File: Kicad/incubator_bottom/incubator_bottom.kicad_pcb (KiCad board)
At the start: 2 copper layers, 99.9 x 73.7 mm, 52 parts, among them J1 Conn_01x02, J10 Conn_01x01, J11 Conn_01x01, J12 Conn_01x01, J2 Conn_02x03_Odd_Even, J4 Conn_01x01, J5 AudioJack3_SwitchTR, J6 AudioJack3_SwitchTR, J7 Conn_01x01, J8 Conn_01x06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

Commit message: fix: PWM for PID
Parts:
- removed logoHackuarium: , Incubator:logoHackuarium
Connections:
- U3 pad 10: FAN -> PID
- U3 pad 11: PID -> D7
- U3 pad 9: D5 -> FAN
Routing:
- net PID: track 121.6 -> 117.6 mm
- net FAN: track 36.1 -> 34.9 mm

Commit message: feat: v1.0.1 of board
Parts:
- added D6: GREEN, LED_SMD:LED_0805_2012Metric_Pad1.15x1.40mm_HandSolder, F.Cu at (95.2, -45.2)
- added D7: RED, LED_SMD:LED_0805_2012Metric_Pad1.15x1.40mm_HandSolder, F.Cu at (97.7, -46.9)
- added R14: 10k, Resistor_SMD:R_0805_2012Metric_Pad1.20x1.40mm_HandSolder, F.Cu at (95.2, -41.0)
- added R15: 10k, Resistor_SMD:R_0805_2012Metric_Pad1.20x1.40mm_HandSolder, F.Cu at (97.7, -41.0)
- added logoHackuarium: , Incubator:logoHackuarium, B.Cu at (86.9, -54.1)
- added logoHackuarium: , Incubator:logoHackuarium, F.Cu at (0.25, -18.9)
- moved C5 7.87 mm to (83.1, -23.6), turned to 270 degrees
- moved H6 2.72 mm to (31.2, -25.6)
- moved H8 2.72 mm to (71.3, -25.6)
- moved JP1 2.43 mm to (81.7, -31.5)
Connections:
- net SCK renamed SCK|MONITORING
- C5 pad 2: GND -> Net-(C5-Pad2)
- J8 pad 1: ~RESET -> Net-(C5-Pad2)
- U3 pad 14: Net-(U3-Pad14) -> ERROR
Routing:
- net ERROR: track 0.00 -> 9.71 mm
- net ~RESET: track 36.1 -> 29.1 mm
- net 12V: track 190.2 -> 184.8 mm
- net Net-(C5-Pad2): track 0.00 -> 5.33 mm
- net Net-(D7-Pad2): track 0.00 -> 3.80 mm
- net ONE-WIRE-2: track 118.2 -> 114.5 mm, vias 4 -> 3
- net SCK|MONITORING: track 20.1 -> 23.5 mm
- net VIN: track 254.1 -> 251.0 mm
- net Net-(D6-Pad2): track 0.00 -> 2.16 mm
- net MOSI: track 19.5 -> 21.0 mm
- net TX: track 14.0 -> 15.3 mm
- net GND: track 9.93 -> 9.51 mm, vias 45 -> 49
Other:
- board text added: "ERR"
- board text added: "Incubator V 1.0.1"
- board text added: "MON"
- board text removed: "Incubator V 1.0.0"

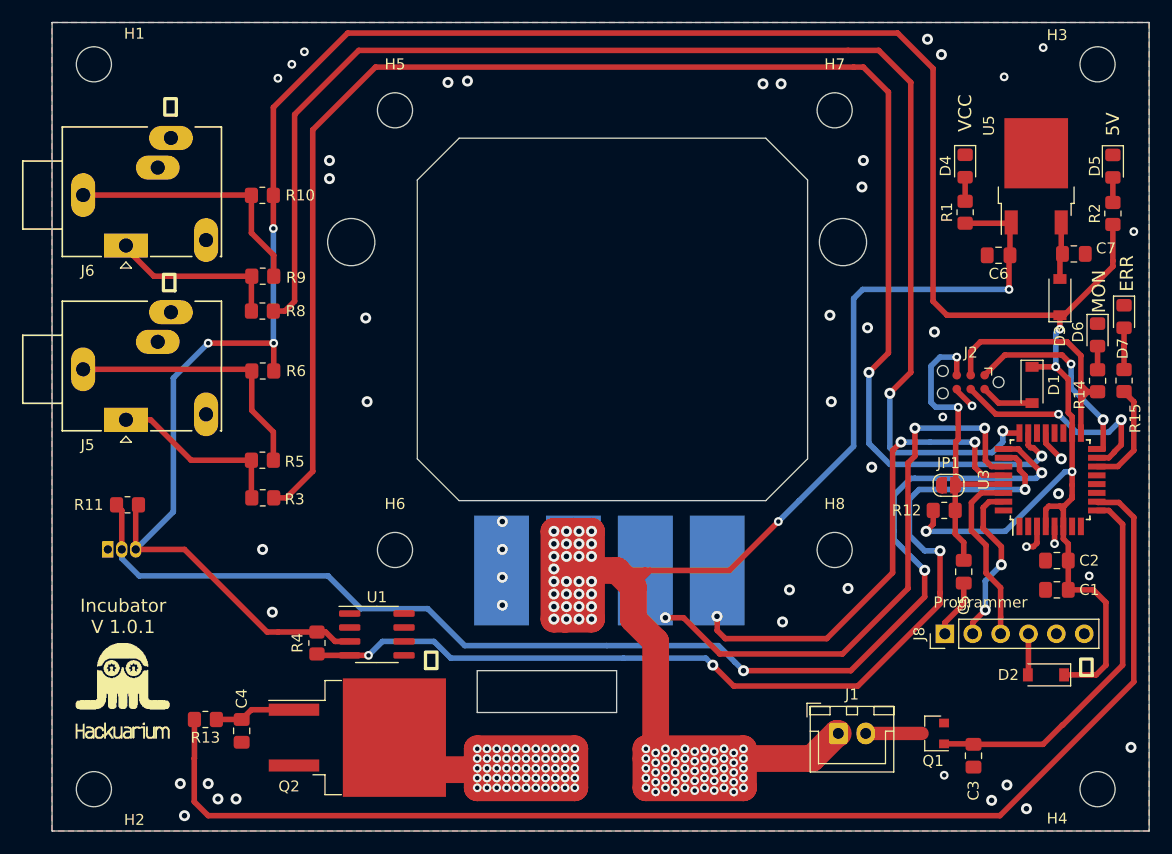
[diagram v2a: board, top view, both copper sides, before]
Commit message: fix: solve issue for holes diameter
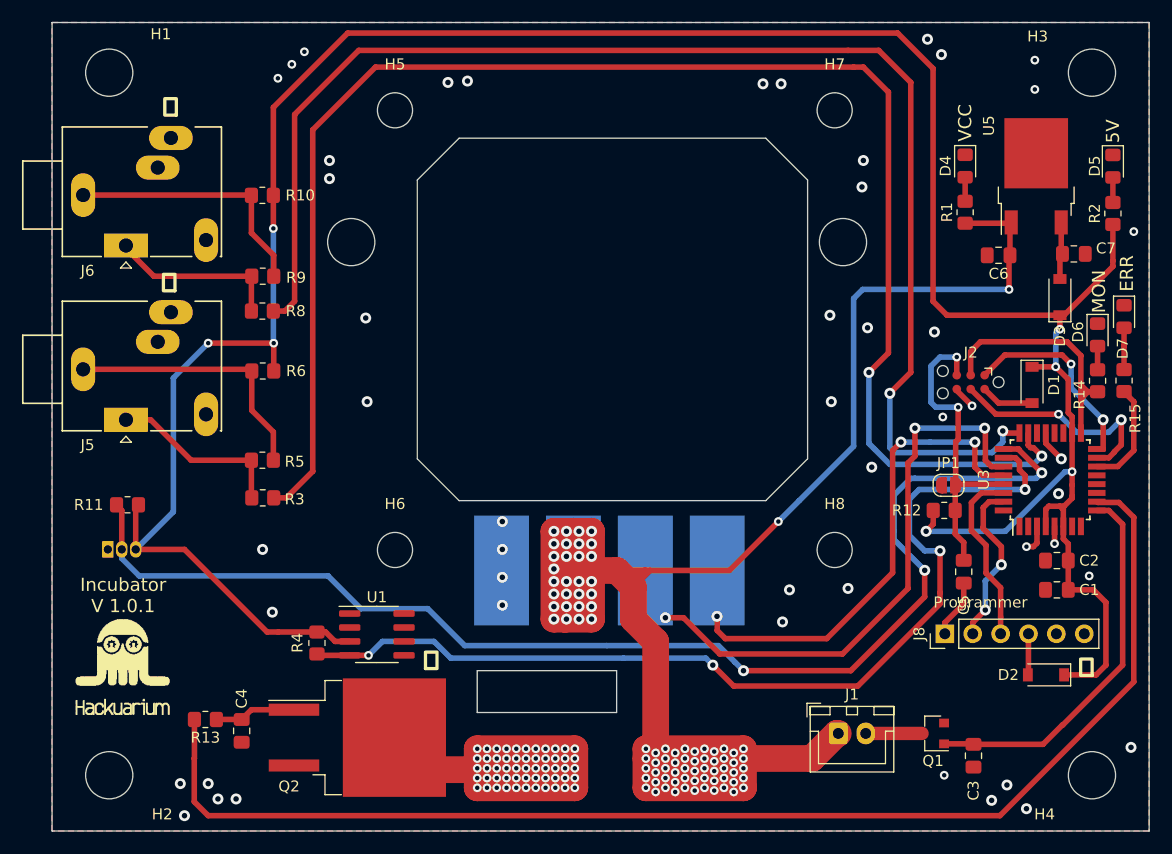
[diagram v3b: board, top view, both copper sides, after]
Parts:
- H1, H2, H3, H4: footprint MountingHole:MountingHole_3.2mm_M3 -> MountingHole:MountingHole_4.3mm_M4
- moved logoHackuarium 2.16 mm to (0.25, -21.1)
- moved H2 1.89 mm to (5.21, -5.08)
- moved H1 1.59 mm to (5.21, -69.1)
- moved H4 1.37 mm to (94.7, -5.08)
- moved H3 0.92 mm to (94.7, -69.1)

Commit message: fix: version 1.0.2 of the PCB change size holes M4 -> M3 and changes their position
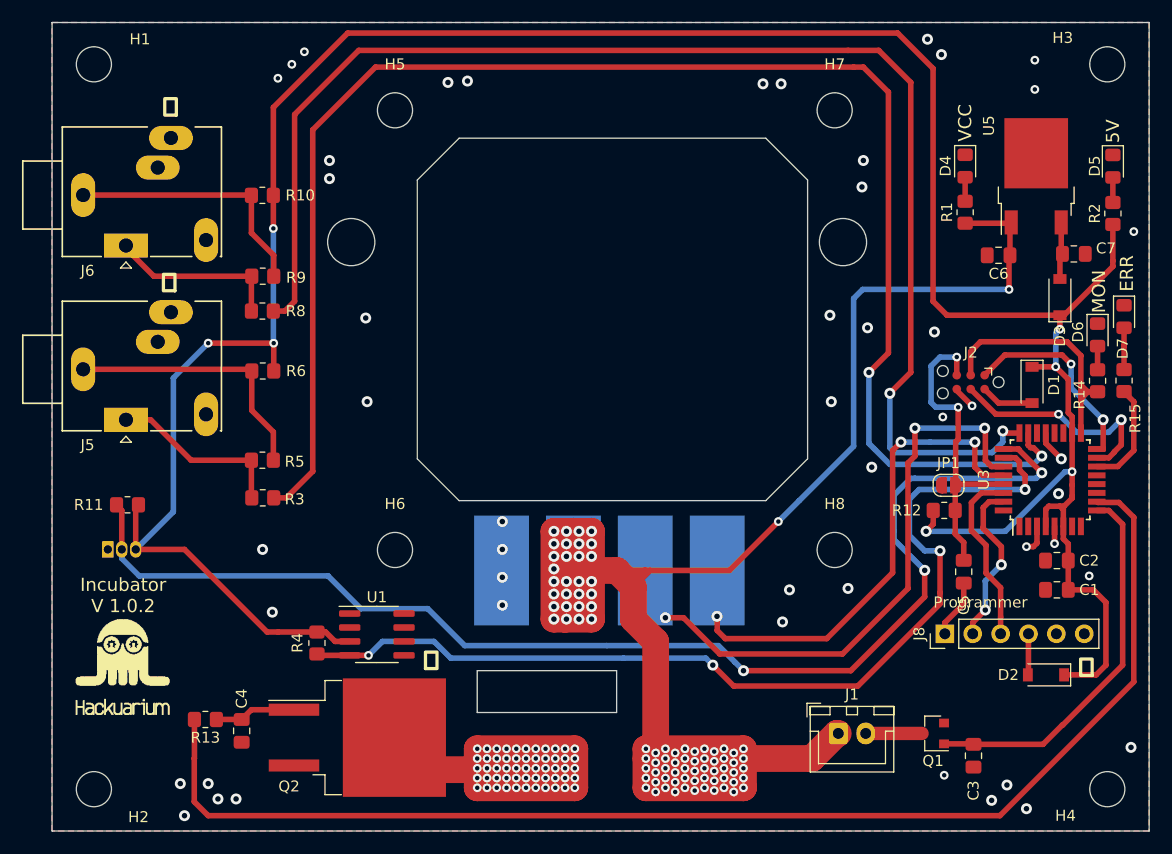
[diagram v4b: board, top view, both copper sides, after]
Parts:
- H1, H2, H3, H4: footprint MountingHole:MountingHole_4.3mm_M4 -> MountingHole:MountingHole_3.2mm_M3
- moved H2 1.89 mm to (3.81, -3.81)
- moved H4 1.89 mm to (96.1, -3.81)
- moved H1 1.59 mm to (3.81, -69.8)
- moved H3 1.59 mm to (96.1, -69.8)
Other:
- board text added: "Incubator V 1.0.2"
- board text removed: "Incubator V 1.0.1"
